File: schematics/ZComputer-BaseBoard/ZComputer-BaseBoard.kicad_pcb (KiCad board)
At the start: 2 copper layers, 268 x 94.5 mm, 23 parts, among them J1 Board to board connector, J10 Board to board connector, J11 Board to board connector, J2 Board to board connector, J3 Board to board connector, J4 Board to board connector, J5 Board to board connector, J6 Board to board connector, J7 Board to board connector, J8 Board to board connector, J9 Conn_micro_USB_board, SW1 RESET_SW

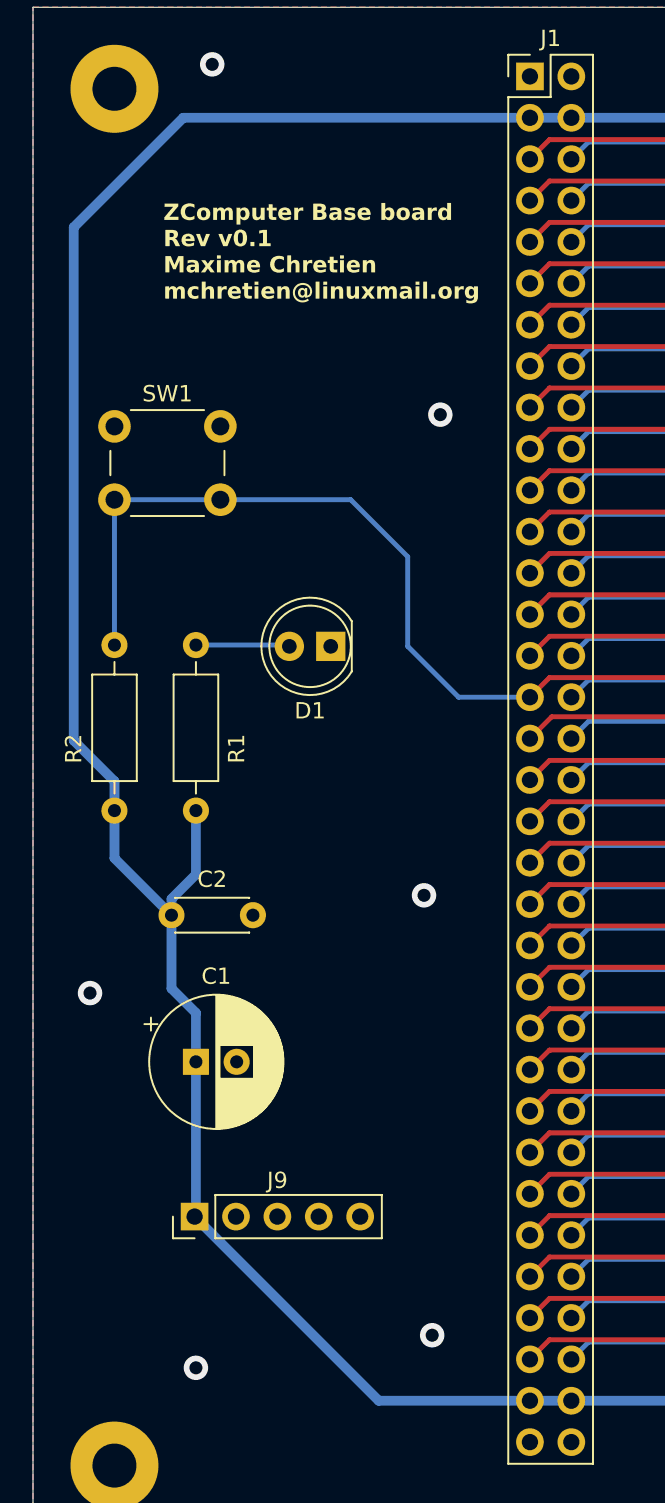
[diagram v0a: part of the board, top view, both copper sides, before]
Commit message: Add power switch on the base board
Signed-off-by: Maxime Chretien <mchretien@linuxmail.org>
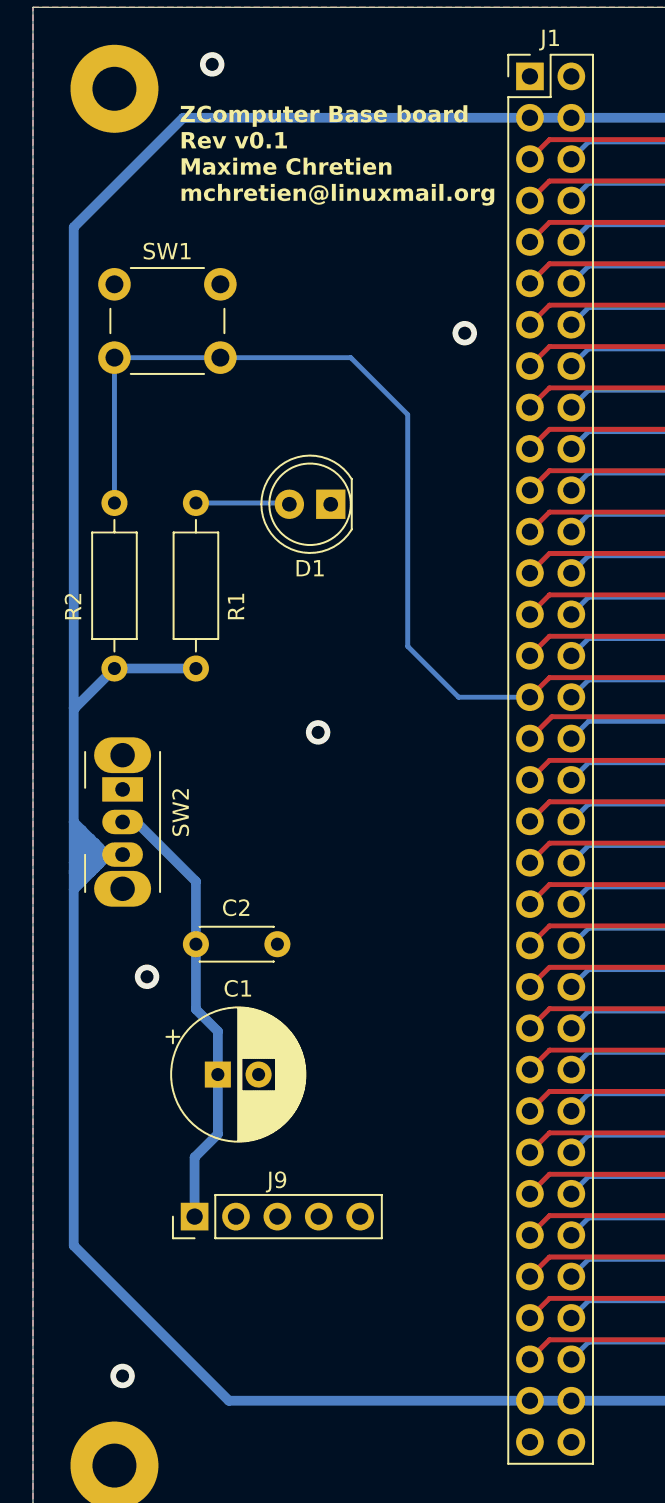
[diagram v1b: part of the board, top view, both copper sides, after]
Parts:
- added SW2: PWR_SW, Button_Switch_THT:SW_Slide_SPDT_Angled_CK_OS102011MA1Q, F.Cu at (20.5, 78.0)
- moved D1 8.72 mm to (33.3, 60.5)
- moved R1 8.72 mm to (25.0, 70.6)
- moved R2 8.72 mm to (20.0, 60.4)
- moved SW1 8.72 mm to (20.0, 47.0)
- moved C2 2.33 mm to (25.0, 87.5)
- moved C1 1.56 mm to (26.3, 95.5)
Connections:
- C1 pad 1: VCC -> 5V
- C2 pad 1: VCC -> 5V
- J1 pad 3: VCC -> /VCC
- J1 pad 4: VCC -> /VCC
- J1 pad 65: VCC -> /VCC
- J1 pad 66: VCC -> /VCC
- J10 pad 3: VCC -> /VCC
- J10 pad 4: VCC -> /VCC
- J10 pad 65: VCC -> /VCC
- J10 pad 66: VCC -> /VCC
- J11 pad 3: VCC -> /VCC
- J11 pad 4: VCC -> /VCC
- J11 pad 65: VCC -> /VCC
- J11 pad 66: VCC -> /VCC
- J2 pad 3: VCC -> /VCC
- J2 pad 4: VCC -> /VCC
- J2 pad 65: VCC -> /VCC
- J2 pad 66: VCC -> /VCC
- J3 pad 3: VCC -> /VCC
- J3 pad 4: VCC -> /VCC
- J3 pad 65: VCC -> /VCC
- J3 pad 66: VCC -> /VCC
- J4 pad 3: VCC -> /VCC
- J4 pad 4: VCC -> /VCC
- J4 pad 65: VCC -> /VCC
- J4 pad 66: VCC -> /VCC
- J5 pad 3: VCC -> /VCC
- J5 pad 4: VCC -> /VCC
- J5 pad 65: VCC -> /VCC
- J5 pad 66: VCC -> /VCC
- J6 pad 3: VCC -> /VCC
- J6 pad 4: VCC -> /VCC
- J6 pad 65: VCC -> /VCC
- J6 pad 66: VCC -> /VCC
- J7 pad 3: VCC -> /VCC
- J7 pad 4: VCC -> /VCC
- J7 pad 65: VCC -> /VCC
- J7 pad 66: VCC -> /VCC
- J8 pad 3: VCC -> /VCC
- J8 pad 4: VCC -> /VCC
- J8 pad 65: VCC -> /VCC
- J8 pad 66: VCC -> /VCC
- J9 pad 1: VCC -> 5V
- R1 pad 1: VCC -> /VCC
- R2 pad 2: VCC -> /VCC
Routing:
- net /VCC: track 0.00 -> 695.8 mm
- net VCC: track 668.4 -> 0.00 mm
- net 5V: track 0.00 -> 28.1 mm
- net /RESET#: track 277.3 -> 286.0 mm
- net GND: vias 6 -> 5
